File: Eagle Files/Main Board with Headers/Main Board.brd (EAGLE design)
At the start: 67 x 43.2 mm, 34 parts, among them Y1 16MHz

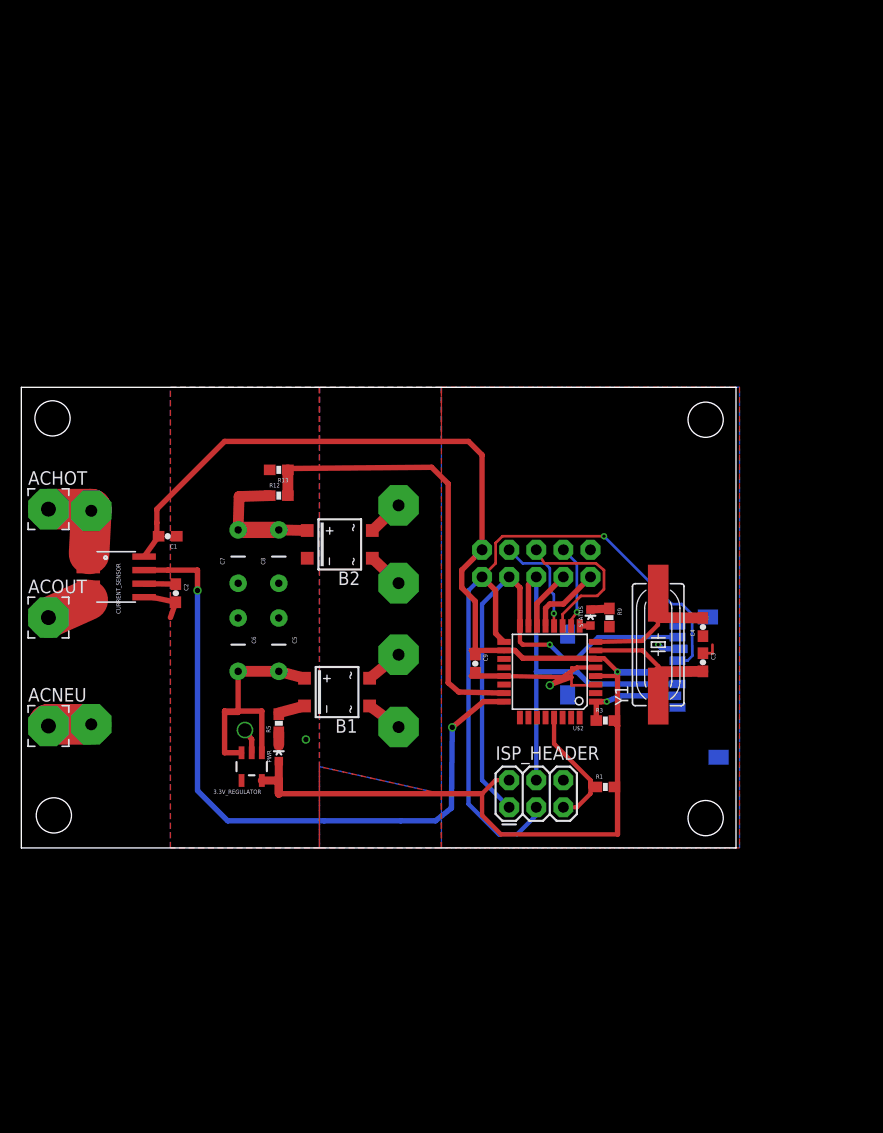
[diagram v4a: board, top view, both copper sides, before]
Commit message: Panelized the Radio board and Main Board.
Basically main Board with Headers is being turned into the new Main Board.
I've already attached the SD Card holder.
Next step is to integrate these two boards, instead of just panelizing them.

--Arthur

git-svn-id: http://cd-net.net/CPE496/trunk@116 05b6d0e0-c345-4a8e-a5b7-579c8bd0b646
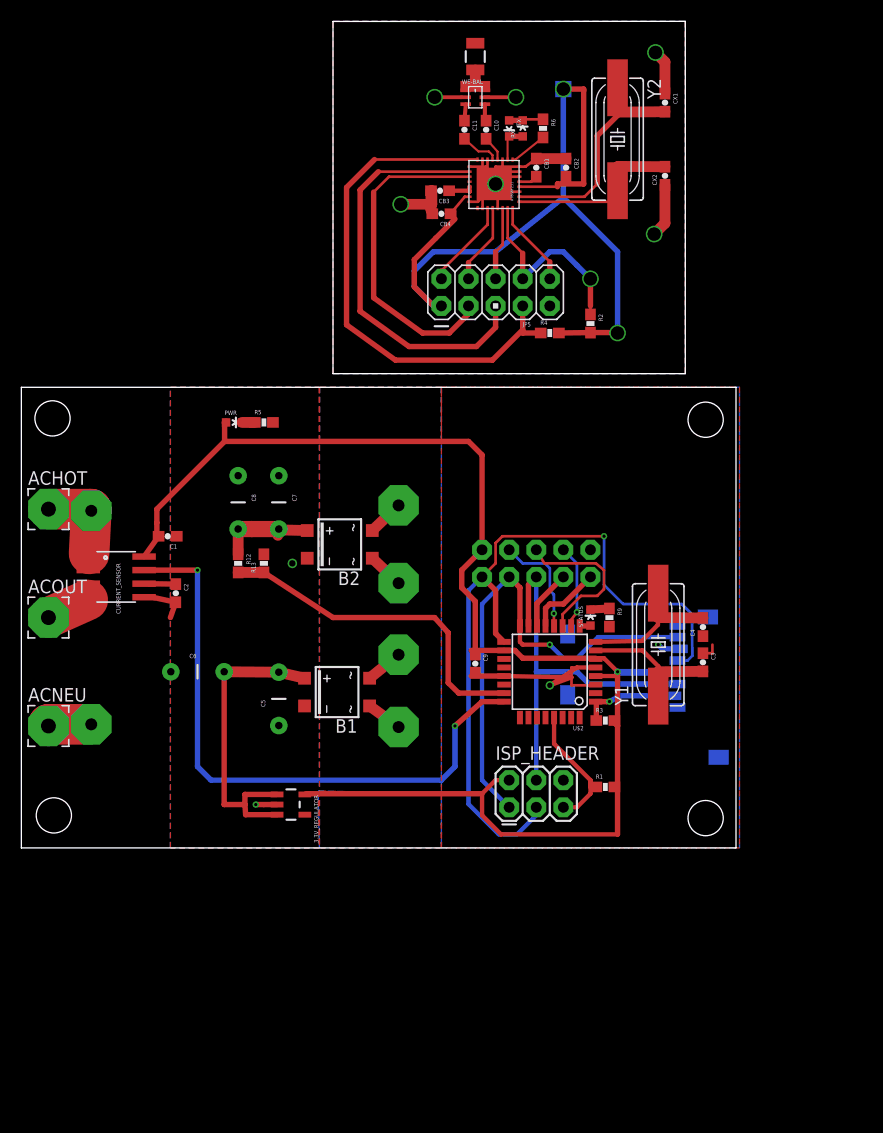
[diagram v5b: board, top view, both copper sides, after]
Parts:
- added C10, C11: 22 pF, SparkFun:0603-CAP
- added CB1, CB2, CB3, CB4: 1 uF, SparkFun:0603-CAP
- added CX1, CX2: 12 pF, SparkFun:0603-CAP
- added JP5: M05X2PTH, SparkFun:AVR_ICSP
- added R2, R4: 10K, SparkFun:0603-RES
- added R6: 100, SparkFun:0603-RES
- added RX: GREEN, SparkFun:LED-0603
- added TX: RED, SparkFun:LED-0603
- added U$3: AT86RF231(RADIO)AT86RF231, group10:32QN2(RADIO)
- added U$4: WE-BAL, group10:WE-BAL
- added U$5: ANTENNA2SMD, SparkFun:ANTENNA-CHIP2
- added Y2: 16 MHZ, group10:HC49UP
- moved PWR 31.3 mm to (19.9, 39.9), turned to 270 degrees
- moved R5 28.2 mm to (22.7, 39.9), turned to 0 degrees
- moved R13 8.87 mm to (22.7, 26.7), turned to 90 degrees
- moved R12 7.41 mm to (20.3, 26.7), turned to 270 degrees
- moved C7 6.35 mm to (24.1, 32.4), turned to 270 degrees
- moved C8 6.35 mm to (20.3, 32.4), turned to 270 degrees
- moved 3.3V_REGULATOR 5.12 mm to (25.3, 4.06), turned to 270 degrees
- moved C5 5.08 mm to (24.1, 14.0), turned to 90 degrees
- moved C6 4.58 mm to (16.5, 16.5), turned to 0 degrees
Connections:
- new net N$10: CB1.2, U$3.AVDD
- new net N$11: CX1.2, U$3.XTAL1, Y2.1
- new net N$12: CX2.2, U$3.XTAL2, Y2.2
- new net N$13: RX.A, TX.C, U$3.DIG4
- new net N$14: R6.1, RX.C, TX.A
- new net N$15: R6.2, U$3.DIG3
- new net N$16: C10.1, U$4.OUT2
- new net N$17: C11.1, U$4.OUT1
- new net N$18: C11.2, U$3.RFN
- new net N$19: C10.2, U$3.RFP
- new net N$20: U$4.IN, U$5.FEED
- new net N$8: CB3.1, U$3.DVDD, U$3.DVDD2
- net 3.3V: now also CB2.2, CB4.1, JP5.1, R2.2, R4.2, U$3.DEVDD, U$3.EVDD
- net CS-RADIO: now also JP5.8, R2.1, U$3./SEL
- net DIG2: now also JP5.5, U$3.DIG2
- net GND: now also CB1.1, CB2.1, CB3.2, CB4.2, CX1.1, CX2.1, JP5.9, U$3.AVSS, U$3.AVSS2, U$3.AVSS3, U$3.AVSS4, U$3.AVSS5, U$3.AVSS6, U$3.DIG1, U$3.DVSS, U$3.DVSS3, U$3.DVSS4, U$3.DVSS5, U$4.GND, U$4.GNDDC
- net IRQ: now also JP5.10, U$3.IRQ
- net MISO: now also JP5.4, U$3.MISO
- net MOSI: now also JP5.6, U$3.MOSI
- net RADIO-RST: now also JP5.7, R4.1, U$3./RST
- net SCK: now also JP5.2, U$3.SCLK
- net SLP_TR: now also JP5.3, U$3.SLP_TR
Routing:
- net 3.3V: track 146.9 -> 225.6 mm, vias 1 -> 3
- net GND: track 36.4 -> 94.7 mm, vias 4 -> 10
- net RADIO-RST: track 7.84 -> 59.3 mm
- net DIG2: track 15.0 -> 53.9 mm
- net SLP_TR: track 10.1 -> 41.0 mm
- net N$11: track 0.00 -> 24.3 mm
- net CS-RADIO: track 5.62 -> 24.6 mm, vias 0 -> 1
- net N$12: track 0.00 -> 17.0 mm
- net SCK: track 68.6 -> 79.7 mm
- net PC0: track 42.8 -> 31.9 mm
- net IRQ: track 7.09 -> 15.2 mm
- net MISO: track 46.8 -> 54.4 mm
- net MOSI: track 37.7 -> 44.6 mm
- net PC1: track 64.3 -> 57.9 mm
- net UNREGULATED_VCC: track 24.4 -> 29.9 mm
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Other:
- board size 67 x 43.2 mm -> 67 x 77.5 mm

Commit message: Cleaned up the Board some in preparation for integration.
TODO:
Fix the Radio Part in the library to reflect the ground plane on the device.
Consider putting either the balun and antenna or the crystal oscilator on the bottom of the board.

--Arthur

git-svn-id: http://cd-net.net/CPE496/trunk@117 05b6d0e0-c345-4a8e-a5b7-579c8bd0b646
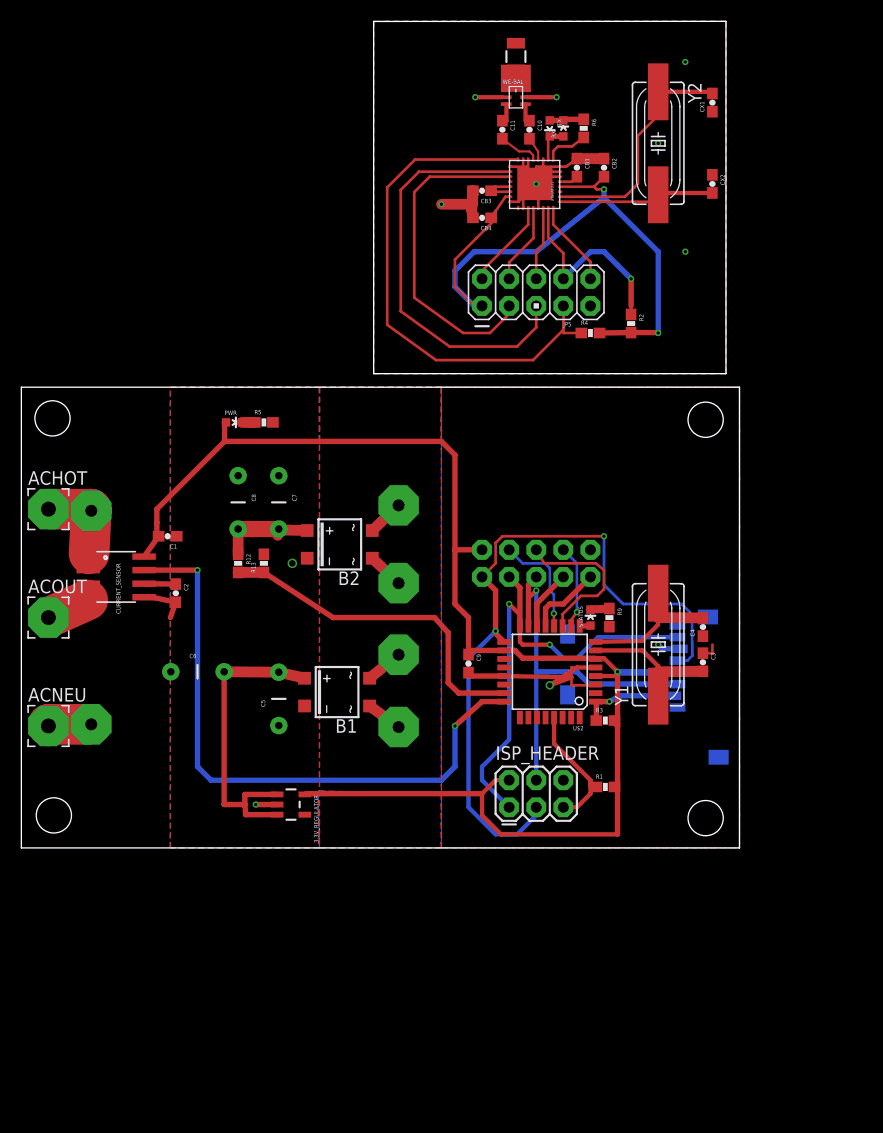
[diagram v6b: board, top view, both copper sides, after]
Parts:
- moved CX2 4.51 mm to (64.8, 62.2), turned to 270 degrees
- moved CX1 4.44 mm to (64.8, 69.8), turned to 90 degrees
- moved C10 4.06 mm to (47.6, 67.3)
- moved CB3 3.94 mm to (43.2, 61.6)
- moved CB4 3.83 mm to (43.2, 59.1)
- moved Y2 3.83 mm to (59.7, 66.0)
- moved CB1 3.81 mm to (52.1, 63.8)
- moved R4 3.81 mm to (53.3, 48.3)
- moved TX 3.81 mm to (49.5, 67.4)
- moved JP5 3.81 mm to (48.3, 52.1)
- moved R2 3.81 mm to (57.1, 49.1)
- moved R6 3.81 mm to (52.7, 67.4)
- moved RX 3.81 mm to (50.8, 67.4)
- moved U$3 3.81 mm to (48.3, 62.2)
- moved U$4 3.81 mm to (46.4, 70.4)
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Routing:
- net 3.3V: track 225.6 -> 203.1 mm
- net GND: track 94.7 -> 80.9 mm, vias 10 -> 11
- net SCK: track 79.7 -> 75.4 mm, vias 1 -> 2
- net N$11: track 24.3 -> 22.5 mm
- net N$12: track 17.0 -> 15.2 mm
- net MOSI: track 44.6 -> 46.1 mm, vias 0 -> 1
- net N$8: track 2.43 -> 3.77 mm
- net N$15: track 3.58 -> 4.11 mm
- net MISO: track 54.4 -> 54.3 mm, vias 1 -> 2
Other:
- board size 67 x 77.5 mm -> 67.3 x 77.5 mm

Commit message: Main Board with Headers is now almost ready.
I'm adding the FTDI Module right now.

TODO:
1.  Double check regulator Datasheet.  I think we're missing a capacitor.
2.  Update Radio Module Schematics to incorporate ground plane.
3.  Check if the hall effect sensor can work linearly at 3.3V
4.  Finish Adding FTDI chip and USB connector.

--Arthur

git-svn-id: http://cd-net.net/CPE496/trunk@119 05b6d0e0-c345-4a8e-a5b7-579c8bd0b646
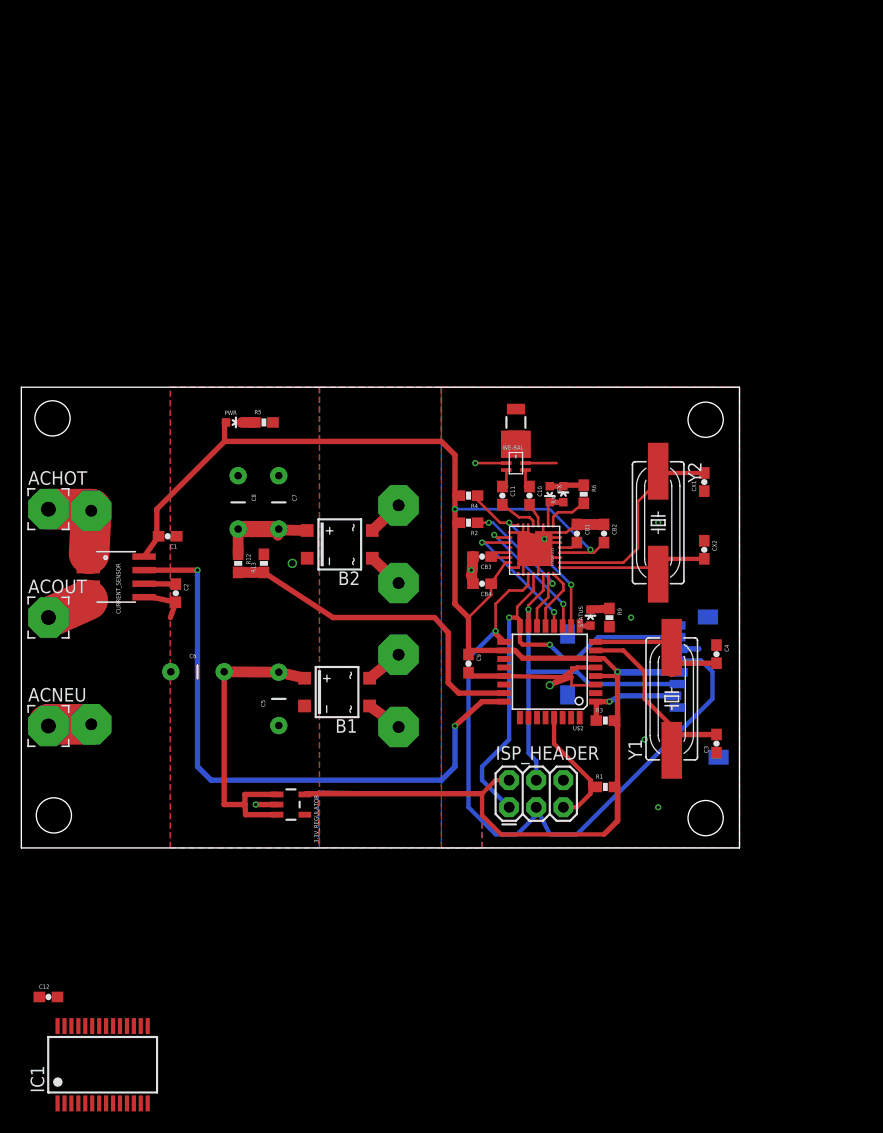
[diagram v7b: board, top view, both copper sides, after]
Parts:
- removed JP5, RADIO-HEADER: M05X2PTH, SparkFun:AVR_ICSP
- added C12: 0.1u, SparkFun:0603-CAP
- added IC1: FT232RL, ftdichip:SSOP28
- moved CX1 35.6 mm to (64.0, 34.3)
- moved Y2 35.6 mm to (59.7, 30.5)
- moved CX2 34.3 mm to (64.0, 27.9)
- moved U$4 34.3 mm to (46.4, 36.1)
- moved U$5 34.3 mm to (46.4, 39.9)
- moved C10 34.3 mm to (47.6, 33.0)
- moved C11 34.3 mm to (45.1, 33.0)
- moved CB1 34.3 mm to (52.1, 29.5)
- moved CB2 34.3 mm to (54.6, 29.5)
- moved CB3 34.3 mm to (43.2, 27.3)
- moved CB4 34.3 mm to (43.2, 24.8)
- moved R6 34.3 mm to (52.7, 33.1)
- moved RX 34.3 mm to (50.8, 33.1)
- moved TX 34.3 mm to (49.5, 33.1)
- moved U$3 34.3 mm to (48.3, 27.9)
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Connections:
- new net VCC: IC1.20
- new net VCCIO: IC1.4
- net 3.3V: now also C12.1; no longer JP5.1, RADIO-HEADER.1
- net CS-RADIO: no longer JP5.8, RADIO-HEADER.8
- net DIG2: no longer JP5.5, RADIO-HEADER.5
- net GND: now also C12.2, IC1.18, IC1.21, IC1.25, IC1.26, IC1.7; no longer JP5.9, RADIO-HEADER.9
- net IRQ: no longer JP5.10, RADIO-HEADER.10
- net MISO: no longer JP5.4, RADIO-HEADER.4
- net MOSI: no longer JP5.6, RADIO-HEADER.6
- net RADIO-RST: no longer JP5.7, RADIO-HEADER.7
- net SCK: no longer JP5.2, RADIO-HEADER.2
- net SLP_TR: no longer JP5.3, RADIO-HEADER.3
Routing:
- net RADIO-RST: track 59.3 -> 17.3 mm, vias 1 -> 2
- net 3.3V: track 203.1 -> 161.9 mm
- net DIG2: track 53.9 -> 12.8 mm, vias 0 -> 2
- net SLP_TR: track 41.0 -> 13.4 mm, vias 1 -> 2
- net SCK: track 75.4 -> 64.7 mm, vias 2 -> 1
- net MISO: track 54.3 -> 44.0 mm
- net MOSI: track 46.1 -> 36.2 mm
- net IRQ: track 15.2 -> 5.96 mm
- net CS-RADIO: track 24.6 -> 15.9 mm, vias 1 -> 2
- net GND: track 80.9 -> 83.9 mm, vias 11 -> 10
- net XTAL1: track 15.8 -> 18.0 mm
- net N$12: track 15.2 -> 17.2 mm
- net N$11: track 22.5 -> 20.8 mm
- net XTAL2: track 15.9 -> 14.6 mm
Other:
- board size 67.3 x 77.5 mm -> 67.3 x 43.2 mm

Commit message: Added USB to Serial Capability to the board.
--Arthur

git-svn-id: http://cd-net.net/CPE496/trunk@122 05b6d0e0-c345-4a8e-a5b7-579c8bd0b646
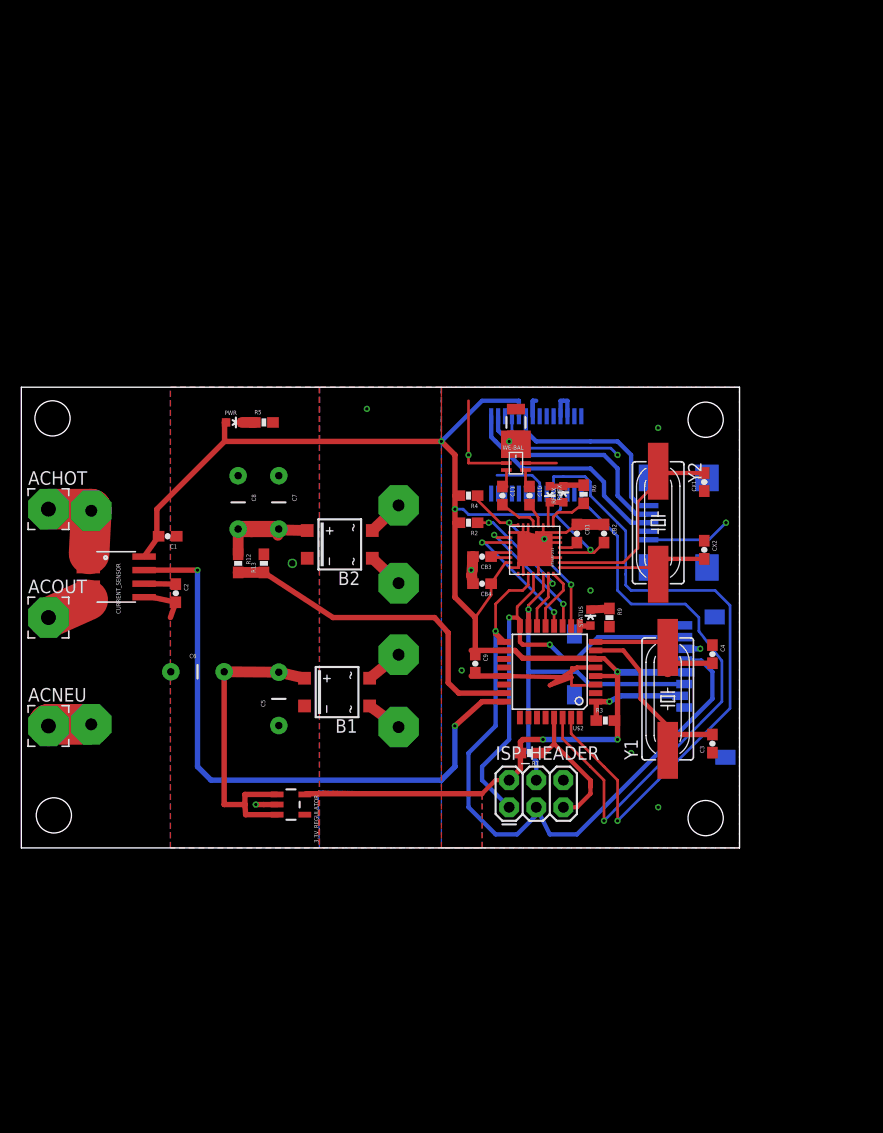
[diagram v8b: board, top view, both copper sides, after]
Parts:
- removed C12: 0.1u, SparkFun:0603-CAP
- added X2: MINI-USB-UX60A-MB-5ST, con-hirose:UX60A-MB-5ST
- moved IC1 70.1 mm to (48.3, 36.8), flipped to the bottom
- moved R1 7.79 mm to (47.6, 8.89), turned to 180 degrees
- moved C9 0.64 mm to (42.5, 17.3)
- moved U$1 0.64 mm to (51.4, 22.1)
- moved C3 0.38 mm to (64.8, 9.78)
- moved C4 0.38 mm to (64.8, 18.2)
- moved Y1 0.38 mm to (60.6, 14.0)
- renumbered RX to RF-RX, TX to RF-TX
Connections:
- removed net VCC: IC1.20
- removed net VCCIO: IC1.4
- new net D+: IC1.15, X2.3
- new net D-: IC1.16, X2.2
- new net RXLED: IC1.22
- new net SERIAL-IN: IC1.1, U$2.30
- new net SERIAL-OUT: IC1.5, U$2.31
- new net TXLED: IC1.23
- new net USBVCC: IC1.20, X2.1
- net 3.3V: now also IC1.19, IC1.4; no longer C12.1
- net GND: now also X2.5; no longer C12.2
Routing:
- net SERIAL-OUT: track 0.00 -> 62.9 mm, vias 0 -> 1
- net SERIAL-IN: track 0.00 -> 54.8 mm, vias 0 -> 1
- net GND: track 83.9 -> 122.1 mm, vias 10 -> 14
- net D+: track 0.00 -> 20.7 mm
- net D-: track 0.00 -> 20.1 mm, vias 0 -> 1
- net USBVCC: track 0.00 -> 18.0 mm
- net RESET: track 12.8 -> 14.1 mm
- net MISO: track 44.0 -> 44.6 mm
- net MOSI: track 36.2 -> 36.8 mm
- net CS-SD_CARD: track 9.21 -> 9.84 mm
- net SCK: track 64.7 -> 64.1 mm
- net 3.3V: track 161.9 -> 162.5 mm, vias 3 -> 6
